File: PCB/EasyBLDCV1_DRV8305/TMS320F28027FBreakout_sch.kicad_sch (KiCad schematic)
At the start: 21 parts, among them J2 TC2050-IDC, U2 TMS320F28027FPTT

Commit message: Fixed Naming Scheme
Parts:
- removed J2: TC2050-IDC, Connector:Tag-Connect_TC2050-IDC-NL_2x05_P1.27mm_Vertical, symbol Connectors:TC2050-IDC
- removed U2: TMS320F28027FPTT, TMS320F28027FPTT:PT0048A_N, symbol TMS320F28027FPTT:TMS320F28027FPTT
- added J2: TC2050-IDC, symbol EasyBLDC:TC2050-IDC
- added U2: TMS320F28027FPTT, EasyBLDC:PT0048A_N, symbol EasyBLDC:TMS320F28027FPTT
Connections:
- net 3.3V: now also J2.1 (Pin_1)
- net COM: now also U2.25 (GPIO19_XCLKIN_SPISTEA_SCIRXDA_ECAP1_N)
- net EN_GATE: now also U2.41 (GPIO6_EPWM4A_EPWMSYNCI_EPWMSYNCO)
- net GND: now also J2.3 (Pin_3), J2.5 (Pin_5), U2.12 (VSSA_VREFLO), U2.33 (VSS), U2.34 (VREGENZ_N), U2.44 (VSS), U2.45 (X1)
- net INH_A: now also U2.29 (GPIO0_EPWM1A)
- net INH_B: now also U2.37 (GPIO2_EPWM2A)
- net INH_C: now also U2.39 (GPIO4_EPWM3A)
- net INL_A: now also U2.28 (GPIO1_EPWM1B_COMP1OUT)
- net INL_B: now also U2.38 (GPIO3_EPWM2B_COMP2OUT)
- net INL_C: now also U2.40 (GPIO5_EPWM3B_ECAP1)
- net LED: now also U2.19 (GPIO34_COMP2OUT)
- net MCU_ISEN_A: now also U2.13 (ADCINB1)
- net MCU_ISEN_B: now also U2.15 (ADCINB3)
- net MCU_ISEN_C: now also U2.18 (ADCINB7)
- net SCLK: now also U2.24 (GPIO18_SPICLKA_SCITXDA_XCLKOUT)
- net SDI: now also U2.27 (GPIO16_SPISIMOA_TZ2_N)
- net SDO: now also U2.26 (GPIO17_SPISOMIA_TZ3_N)
- net TCK: now also J2.4 (Pin_4), U2.23 (GPIO38_XCLKIN_TCK)
- net TDI: now also J2.8 (Pin_8), U2.20 (GPIO35_TDI)
- net TDO: now also J2.6 (Pin_6), U2.22 (GPIO37_TDO)
- net TMS: now also J2.2 (Pin_2), U2.21 (GPIO36_TMS)
- net VDDA: now also U2.11 (VDDA)
- net VDDIO: now also U2.35 (VDDIO)
- net VSEN_A: now also U2.6 (ADCINA7)
- net VSEN_B: now also U2.7 (ADCINA3)
- net VSEN_C: now also U2.8 (ADCINA1)
- net VSEN_PVDD: now also U2.10 (ADCINA0_VREFHI)
- net WAKE: now also U2.42 (GPIO7_EPWM4B_SCIRXDA)
- net nFAULT: now also U2.48 (GPIO28_SCIRXDA_SDAA_TZ2_N)
- net nSCS: now also U2.36 (GPIO33_SCLA_EPWMSYNCO_ADCSOCBO_N)
- net nTRST: now also J2.9 (Pin_9), U2.2 (TRST_N)
- net nXRS: now also U2.3 (XRS_N)
- net at C29.1: now also U2.32 (VDD)
- net at C30.1: now also U2.43 (VDD)

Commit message: Updated Schematic With Missing Footprints
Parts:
- D2: footprint (none) -> LED_SMD:LED_0805_2012Metric
- J2: footprint (none) -> EasyBLDC:Tag-Connect_TC2050-IDC-NL_2x05_P1.27mm_Vertical
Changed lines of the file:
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@@
 			)
 		)
-		(property "Footprint" ""
+		(property "Footprint" "LED_SMD:LED_0805_2012Metric"
 			(at 261.62 86.36 0)
 			(effects
@@
 			)
 		)
-		(property "Footprint" ""
+		(property "Footprint" "EasyBLDC:Tag-Connect_TC2050-IDC-NL_2x05_P1.27mm_Vertical"
 			(at 236.22 45.72 0)
 			(effects

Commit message: Progress on MCU Breakout
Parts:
- COM1: footprint TestPoint:TestPoint_Pad_D3.0mm -> TestPoint:TestPoint_Pad_D2.0mm
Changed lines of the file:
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@@
 			)
 		)
-		(property "Footprint" "TestPoint:TestPoint_Pad_D3.0mm"
+		(property "Footprint" "TestPoint:TestPoint_Pad_D2.0mm"
 			(at 190.5 85.09 0)
 			(effects

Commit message: Updated Inductor and excluded tps from BOM
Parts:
- COM1, J2: now left out of the parts list
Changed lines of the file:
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@@
 		(unit 1)
 		(exclude_from_sim no)
-		(in_bom yes)
+		(in_bom no)
 		(on_board yes)
 		(dnp no)
@@
 		(unit 1)
 		(exclude_from_sim no)
-		(in_bom yes)
-		(on_board yes)
-		(dnp no)
+		(in_bom no)
+		(on_board yes)
+		(dnp no)

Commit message: Fixed errors with silkscreen overlaping vias. Generated final gerbers.
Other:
- company: Buckley Boards  -> Peter Buckley Engineering
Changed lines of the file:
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@@
 		(date "2024-08-06")
 		(rev "1.0")
-		(company "Buckley Boards ")
+		(company "Peter Buckley Engineering")
 	)
 	(junction

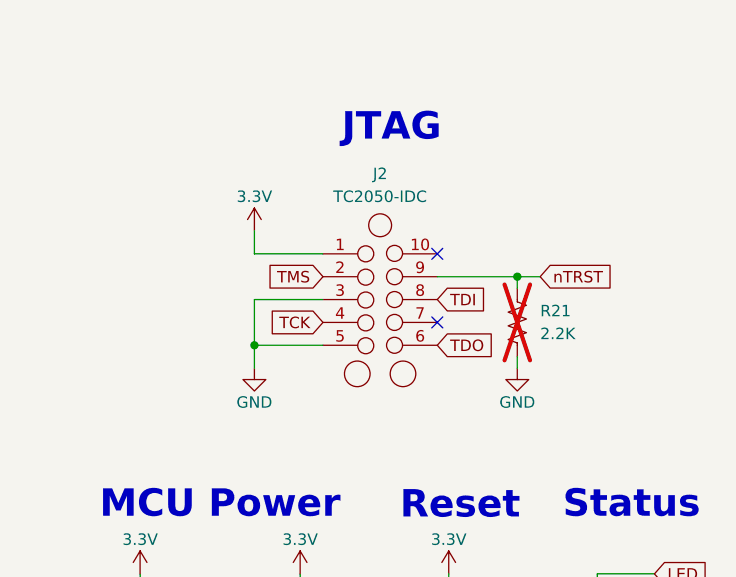
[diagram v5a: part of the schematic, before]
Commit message: JTAG Connector Changed
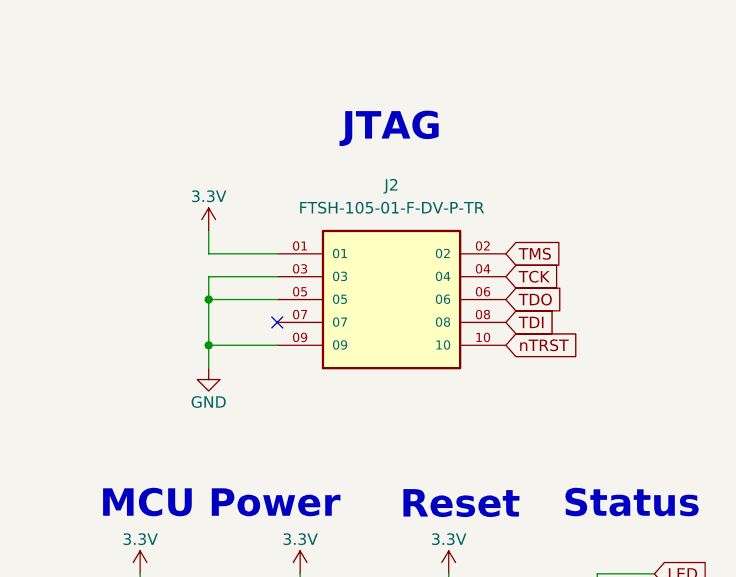
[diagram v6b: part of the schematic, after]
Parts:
- removed J2: TC2050-IDC, EasyBLDC:Tag-Connect_TC2050-IDC-NL_2x05_P1.27mm_Vertical, symbol EasyBLDC:TC2050-IDC
- removed R21: 2.2K, Resistor_SMD:R_0603_1608Metric, symbol Device:R_US
- added J2: FTSH-105-01-F-DV-P-TR, EasyBLDC:SAMTEC_FTSH-105-01-F-DV-P-TR, symbol EasyBLDC:FTSH-105-01-F-DV-P-TR
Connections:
- net 3.3V: now also J2.01
- net GND: now also J2.03, J2.05, J2.09
- net TCK: now also J2.04
- net TDI: now also J2.08
- net TDO: now also J2.06
- net TMS: now also J2.02
- net nTRST: now also J2.10
- no-connect marks 13 -> 12
